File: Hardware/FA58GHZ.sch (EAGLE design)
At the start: 16 parts, among them U1 ATMEGA328P_TQFP, Y1 16MHZ

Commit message: Backup: Working in the Schematic, Footprints and PCB
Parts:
- added C10, C8, C9: 0.1uF, resistor:C-EUC0603
- added IC1: MAX4311EEE, maxim:MAX4311EEE
- added JP3: (no value), SparkFun-Connectors:M06SILK_FEMALE_PTH
- added JP4: (no value), SparkFun-Connectors:M04PTH
- added R10, R11, R12: 1k, resistor:R-US_R0603
- added R5, R6, R7: 10k, resistor:R-US_R0603
- added R8: 470, resistor:R-US_R0603
- added R9: 5k1, resistor:R-US_R0603
- added SG1: BUZZERSMD, SparkFun-Electromechanical:BUZZERSMD
- added U2: RX5808, FreakyAttic-EagleLibrary:RX5808
- added X1: SMA, con-coax:SMA-142-0701-881/886
- JP1: device SparkFun-Connectors:M03PTH -> SparkFun-Connectors:M03SMD
- R3, R4: value 10k -> ?
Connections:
- new net BUT1: U1.PD2(INT0)-D2
- new net BUT2: U1.PD3(INT1)-D3
- new net CH1: R7.1, U1.PB2(SS/OC1B)-D10
- new net CH2: R5.1, U1.PB3(MOSI/OC2)-D11
- new net CH3: R6.1, U1.PB4(MISO)-D12
- new net LED: R2.2, U1.PB5(SCK)-D13
- new net N$10: R12.1, U1.PD5(T1)-D5
- new net N$11: SG1.2, U1.PD6(AIN0)-D6
- new net N$12: R12.2, SG1.1
- new net N$13: R6.2, U2.CH1
- new net N$14: R5.2, U2.CH2
- new net N$15: R7.2, U2.CH3
- new net N$16: U2.ANT, X1.1
- new net N$7: R9.1, U1.PB1(OC1A)-D9
- new net N$8: R10.1, U1.PD0(RXD)-D0
- new net N$9: R11.1, U1.PD1(TXD)-D1
- new net OSD: IC1.IN0, R8.2, R9.2
- new net RSSI1: JP4.2, U1.ADC6-A6, U2.RSSI
- new net RSSI2: JP4.4, U1.ADC7-A7
- new net SEL0: IC1.A0
- new net SEL1: IC1.A1
- new net VIDEO1: IC1.IN1, JP3.2, U2.VIDEO
- new net VIDEO2: IC1.IN2, JP3.4
- new net VIDEO3: IC1.IN3, JP3.6
- new net VIDEO_OUT: IC1.FB, IC1.OUT
- net AN_VPOW: now also C9.2
- net GND: now also C10.1, C8.2, C9.1, IC1.V-, JP3.1, JP3.3, JP3.5, JP4.1, JP4.3, U2.GND@1, U2.GND@2, U2.GND@3, U2.GND@4, X1.2
- net N$6: now also R8.1, U1.PD7(AIN1)-D7; no longer R2.2, U1.PB5(SCK)
- net VCC: now also C10.2, C8.1, IC1.!SHDN, IC1.V+, U2.+5V
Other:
- note added: "1.0"
- note added: "A 5.8GHz video receiver module with OSD menu and multiple video inputs."
- note added: "FA58GHZ.sch"
- moved on the sheet: C1, C4, C5, D1, R1, R2, U1, Y1

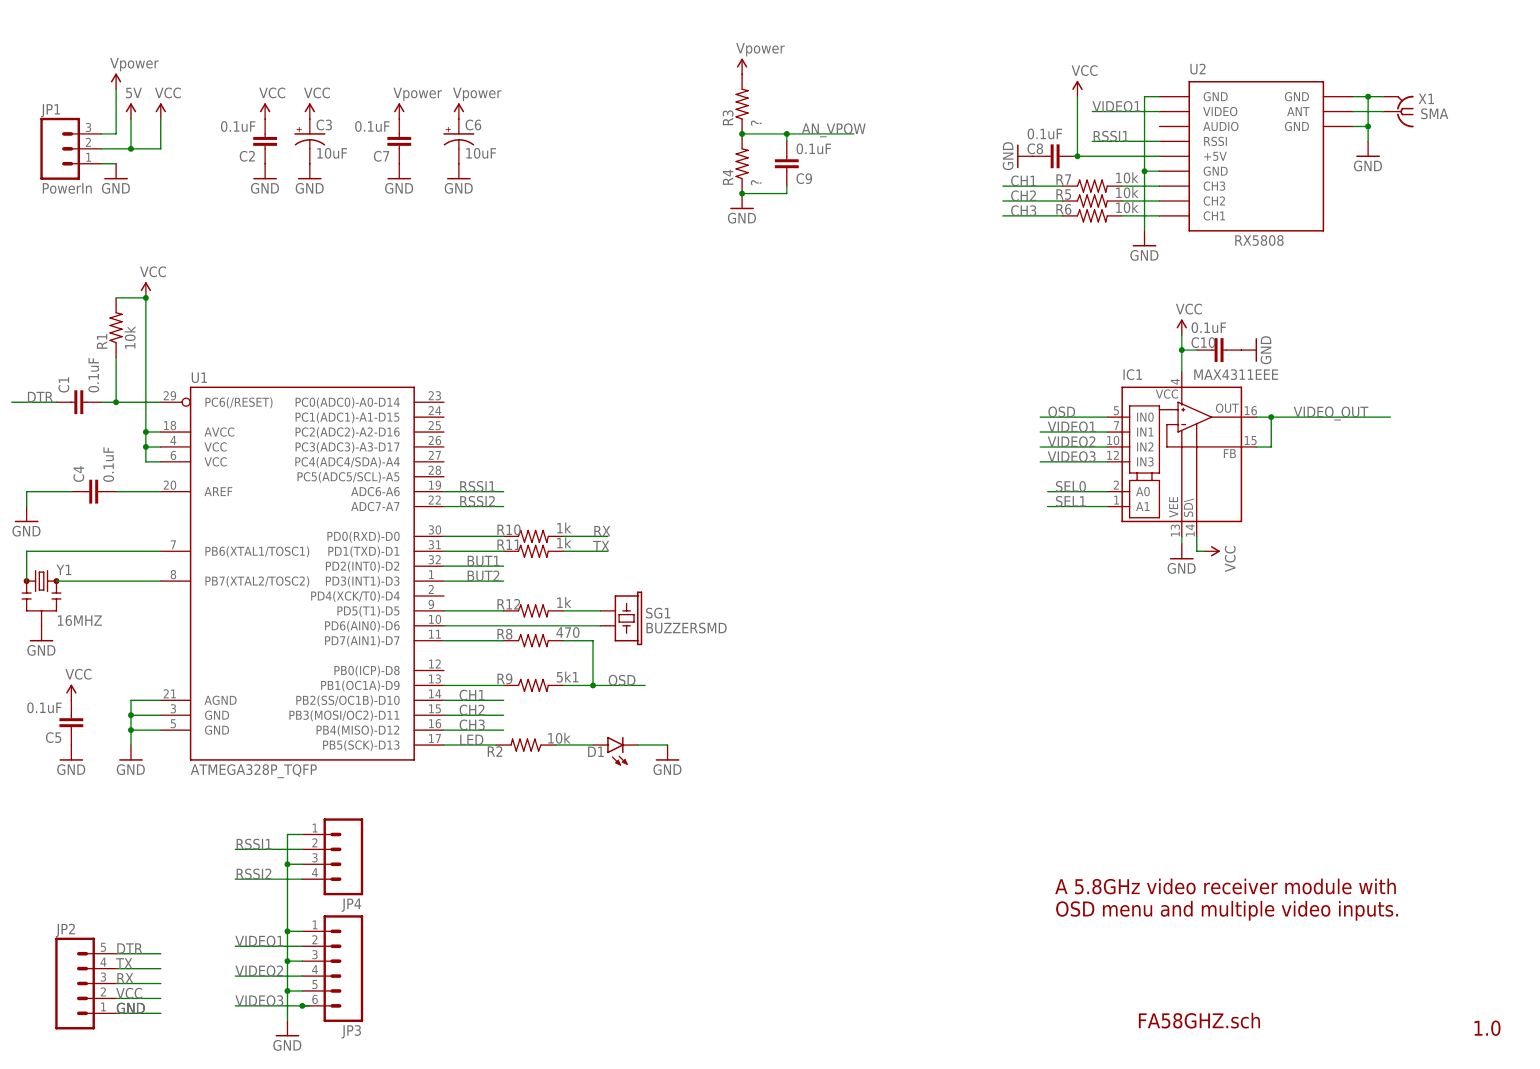
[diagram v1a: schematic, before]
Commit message: Finish with the board Schematic, starting to code functions.
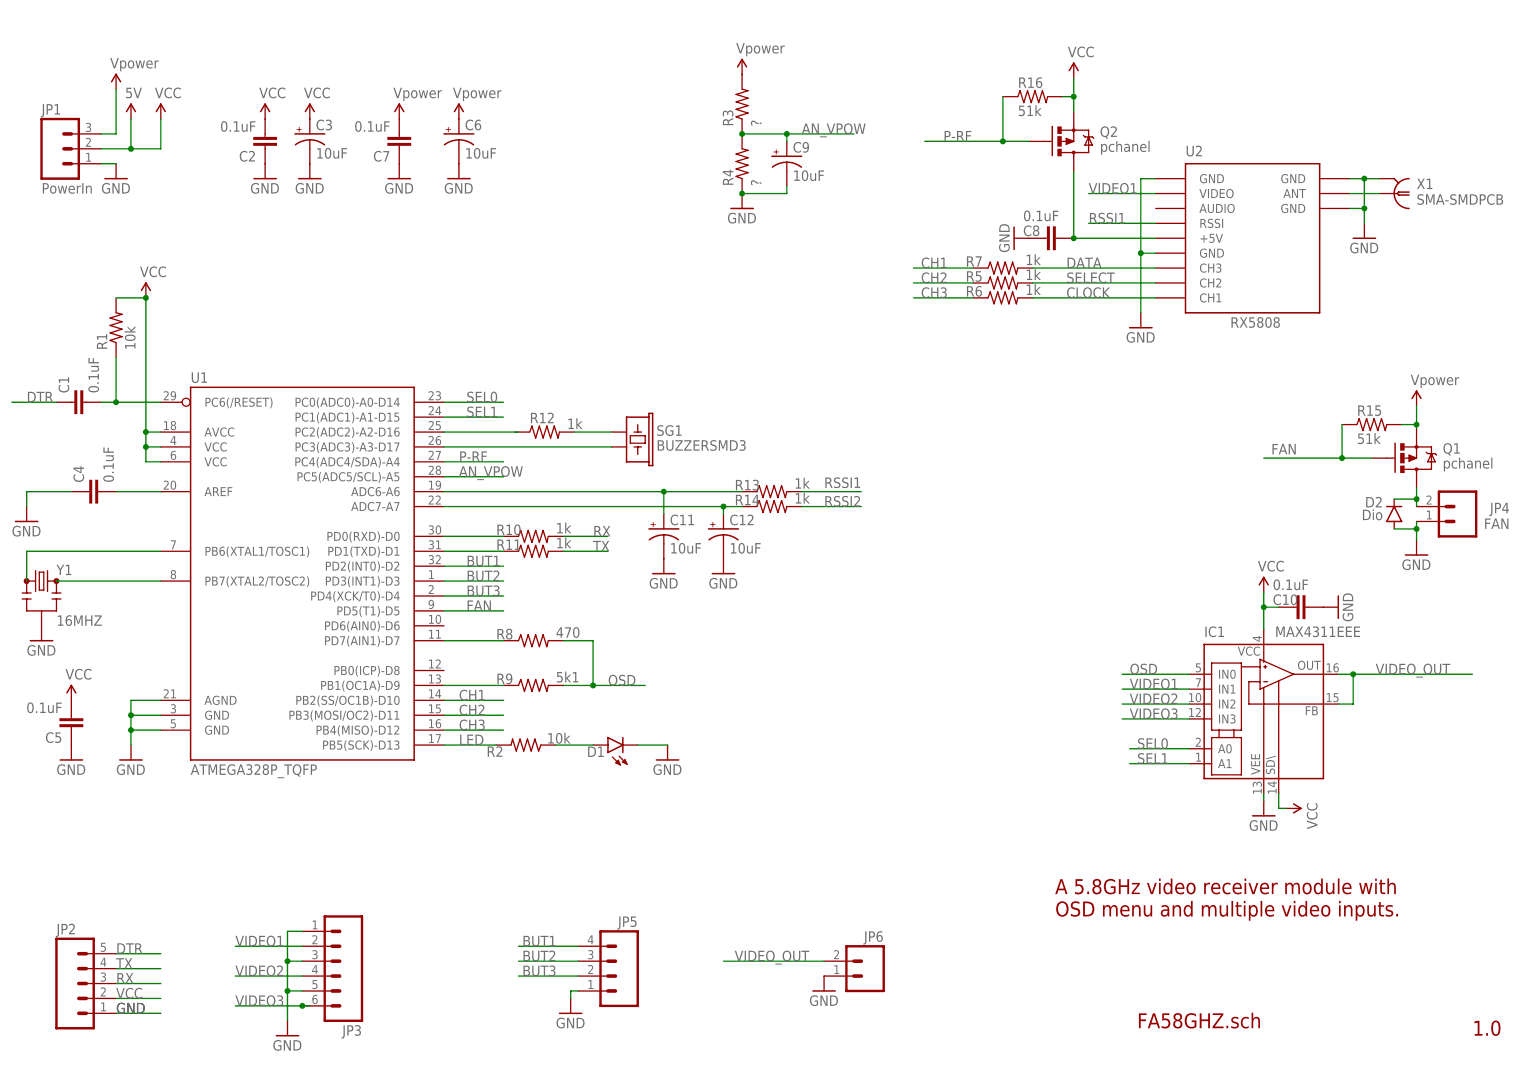
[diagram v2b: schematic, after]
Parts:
- added C11, C12: 10uF, SparkFun-Capacitors:10UF-16V-10%(TANT)
- added D2: Dio, SparkFun-DiscreteSemi:DIODEBAS16
- added JP5: (no value), SparkFun-Connectors:M04PTH
- added JP6: (no value), SparkFun-Connectors:M02PTH
- added Q1, Q2: pchanel, SparkFun-DiscreteSemi:MOSFET-PCHANNEL
- added R13, R14: 1k, resistor:R-US_R0603
- added R15, R16: 51k, resistor:R-US_R0603
- C9: value 0.1uF -> 10uF; device resistor:C-EUC0603 -> SparkFun-Capacitors:10UF-16V-10%(TANT)
- JP4: value (none) -> FAN; device SparkFun-Connectors:M04PTH -> FreakyAttic-EagleLibrary:M02PTH
- R5, R6, R7: value 10k -> 1k
- SG1: value BUZZERSMD -> BUZZERSMD3; device SparkFun-Electromechanical:BUZZERSMD -> FreakyAttic-EagleLibrary:BUZZERSMD3
- X1: value SMA -> SMA-SMDPCB; device con-coax:SMA-142-0701-881/886 -> FreakyAttic-EagleLibrary:SMA-SMDPCB
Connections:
- net N$13 renamed CLOCK
- net N$14 renamed SELECT
- net N$15 renamed DATA
- removed net RSSI2: JP4.4, U1.ADC7-A7
- new net BUT3: JP5.2
- new net FAN: Q1.G, R15.1
- new net N$17: C12.+, R14.1, U1.ADC7-A7
- new net N$18: C11.+, R13.1, U1.ADC6-A6
- new net N$19: D2.C, JP4.2, Q1.D
- new net N$20: C8.1, Q2.D, U2.+5V
- new net P-RF: Q2.G, R16.1
- net AN_VPOW: now also C9.+; no longer C9.2
- net BUT1: now also JP5.4
- net BUT2: now also JP5.3
- net GND: now also C11.-, C12.-, C9.-, D2.A, JP5.1, JP6.1; no longer C9.1, JP4.3
- net N$10: now also U1.PC2(ADC2)-A2-D16; no longer R12.1, U1.PD5(T1)-D5
- net N$11: now also U1.PC3(ADC3)-A3-D17; no longer U1.PD6(AIN0)-D6
- net RSSI1: no longer JP4.2, U1.ADC6-A6
- net VCC: now also Q1.S, Q2.S, R15.2, R16.2; no longer C8.1, U2.+5V
- net VIDEO_OUT: now also JP6.2
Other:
- moved on the sheet: C10, C8, IC1, R12, R5, R6, R7, SG1, U2

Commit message: Backup: Implemented OSD menu for Battery Monitor, needs to test it. - Modifications for the schematic - working on the PCB
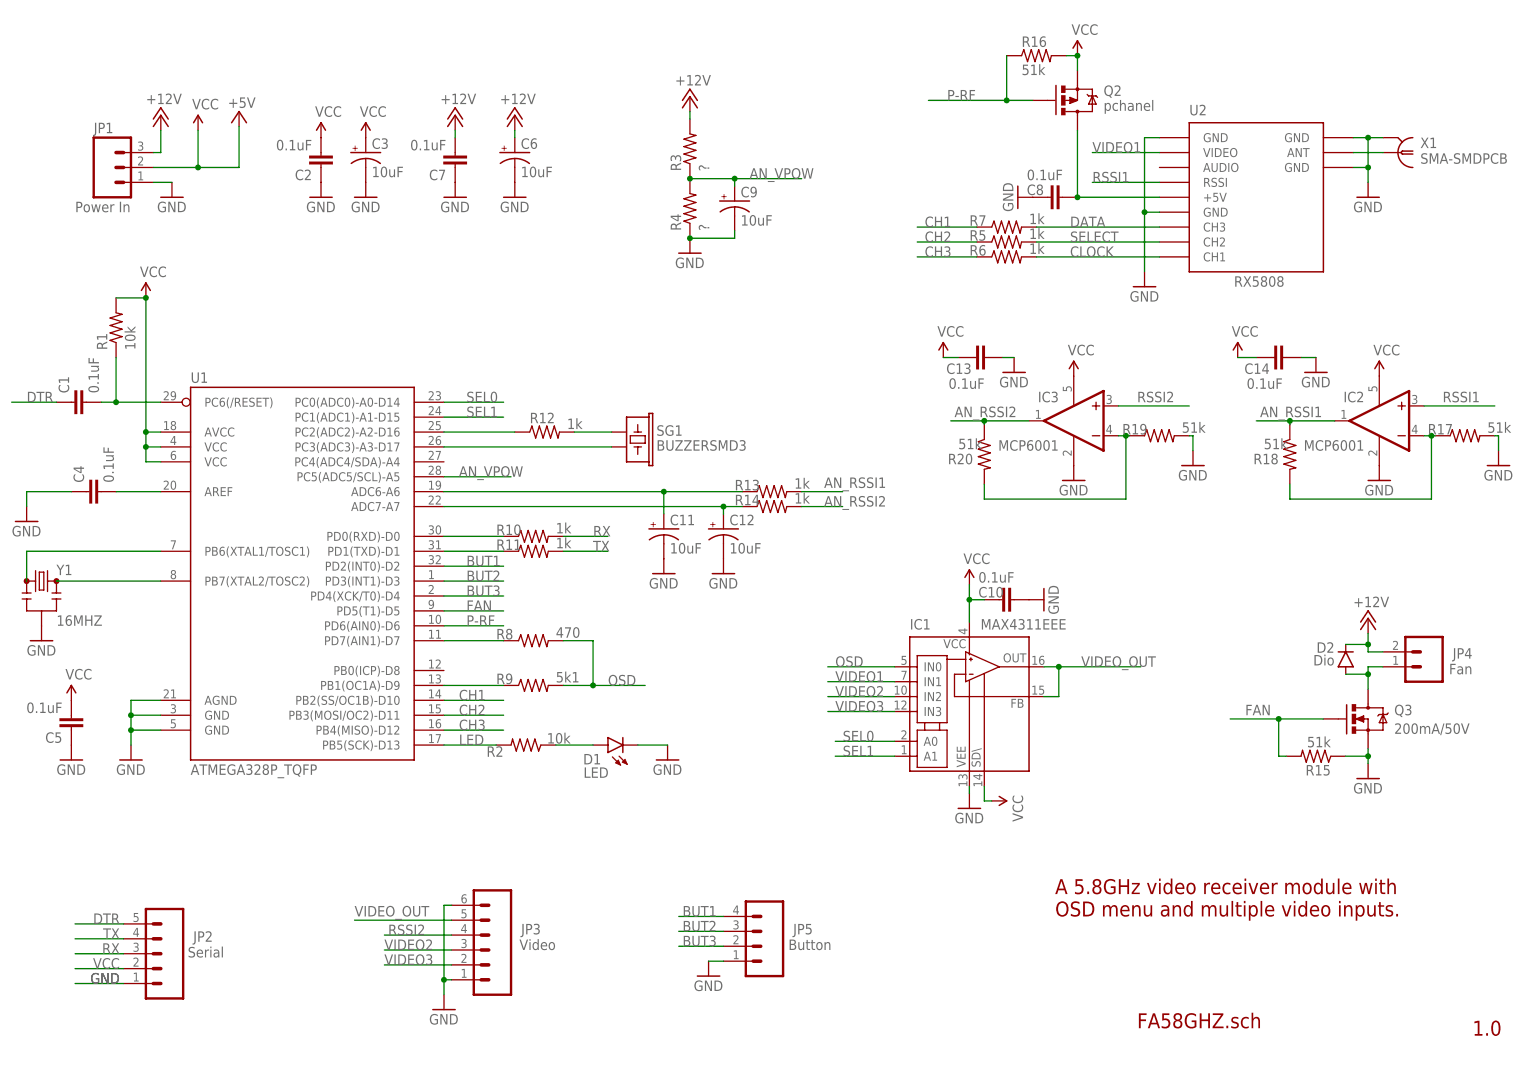
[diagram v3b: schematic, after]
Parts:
- removed JP6: (no value), SparkFun-Connectors:M02PTH
- removed Q1: pchanel, SparkFun-DiscreteSemi:MOSFET-PCHANNEL
- added C13, C14: 0.1uF, resistor:C-EUC0603
- added IC2, IC3: MCP6001, linear:MCP601OT
- added Q3: 200mA/50V, SparkFun-DiscreteSemi:MOSFET-NCHANNELBSS138
- added R17, R18, R19, R20: 51k, resistor:R-US_R0603
- D1: value (none) -> LED
- JP1: value PowerIn -> Power In; device SparkFun-Connectors:M03SMD -> FreakyAttic-EagleLibrary:M03
- JP2: value (none) -> Serial; device SparkFun-Connectors:M05PTH -> FreakyAttic-EagleLibrary:M05
- JP3: value (none) -> Video; device SparkFun-Connectors:M06SILK_FEMALE_PTH -> FreakyAttic-EagleLibrary:M06
- JP4: value FAN -> Fan; device FreakyAttic-EagleLibrary:M02PTH -> FreakyAttic-EagleLibrary:M02
- JP5: value (none) -> Button; device SparkFun-Connectors:M04PTH -> FreakyAttic-EagleLibrary:M04
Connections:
- removed net N$19: D2.C, JP4.2, Q1.D
- new net +12V: C6.+, C7.2, D2.C, JP1.3, JP4.2, R3.2
- new net +5V: JP1.2
- new net AN_RSSI1: IC2.OUT, R13.2, R18.1
- new net AN_RSSI2: IC3.OUT, R14.2, R20.1
- new net N$13: D2.A, JP4.1, Q3.D
- new net N$14: IC2.-IN, R17.1, R18.2
- new net N$15: IC3.-IN, R19.1, R20.2
- new net RSSI2: IC3.+IN, JP3.4
- net AN_VPOW: now also U1.PC5(ADC5/SCL)-A5
- net BUT3: now also U1.PD4(XCK/T0)-D4
- net FAN: now also Q3.G, R15.2, U1.PD5(T1)-D5; no longer Q1.G, R15.1
- net GND: now also C13.2, C14.2, IC2.V-, IC3.V-, JP3.6, Q3.S, R15.1, R17.2, R19.2; no longer D2.A, JP3.3, JP3.5, JP4.1, JP6.1
- net N$10: now also R12.1
- net P-RF: now also U1.PD6(AIN0)-D6
- net RSSI1: now also IC2.+IN
- net RX: now also R10.2
- net SEL0: now also U1.PC0(ADC0)-A0-D14
- net SEL1: now also U1.PC1(ADC1)-A1-D15
- net TX: now also R11.2
- net VCC: now also C13.1, C14.1, IC2.V+, IC3.V+; no longer C6.+, C7.2, JP1.2, JP1.3, Q1.S, R15.2, R3.2
- net VIDEO1: no longer JP3.2
- net VIDEO2: now also JP3.3; no longer JP3.4
- net VIDEO3: now also JP3.2; no longer JP3.6
- net VIDEO_OUT: now also JP3.5; no longer JP6.2
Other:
- moved on the sheet: C10, C2, C3, C6, C7, C8, C9, D2, IC1, JP1, JP2, JP3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

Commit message: Backup: PCB routing finished, need to run DRC
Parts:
- C11, C12, C9: device SparkFun-Capacitors:10UF-16V-10%(TANT) -> SparkFun-Passives:CAP0603-CAP
- Y1: device SparkFun-FreqCtrl:RESONATOR16MHZ -> FreakyAttic-EagleLibrary:OSCILLATOR16MHZ
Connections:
- removed net +5V: JP1.2
- net AN_VPOW: now also C9.1; no longer C9.+
- net BUT1: now also JP5.2; no longer JP5.4
- net BUT3: now also JP5.4; no longer JP5.2
- net GND: now also C11.2, C12.2, C9.2; no longer C11.-, C12.-, C9.-
- net N$17: now also C12.1; no longer C12.+
- net N$18: now also C11.1; no longer C11.+
- net RSSI2: now also JP3.5; no longer JP3.4
- net VCC: now also JP1.2
- net VIDEO2: now also JP3.2; no longer JP3.3
- net VIDEO3: now also JP3.3; no longer JP3.2
- net VIDEO_OUT: now also JP3.4; no longer JP3.5

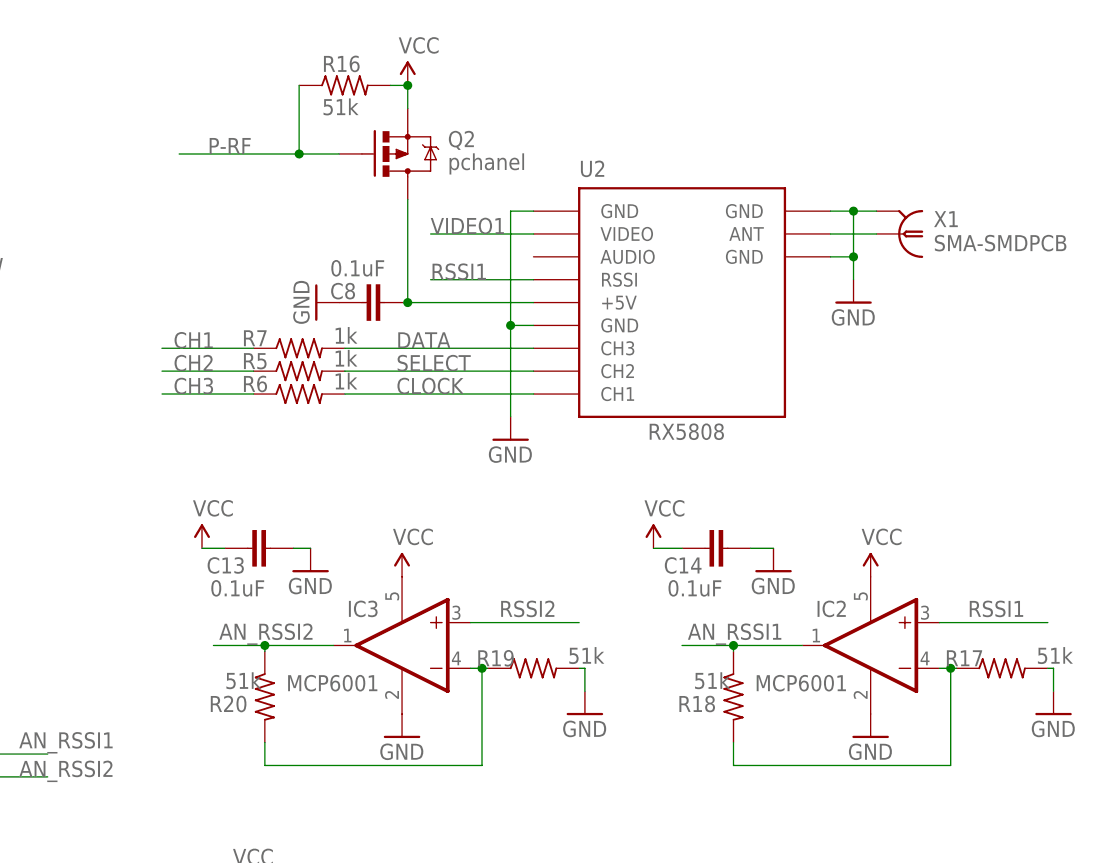
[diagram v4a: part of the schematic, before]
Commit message: BOARD VER: 1.1 - Fix footprints and pinout problems with RF
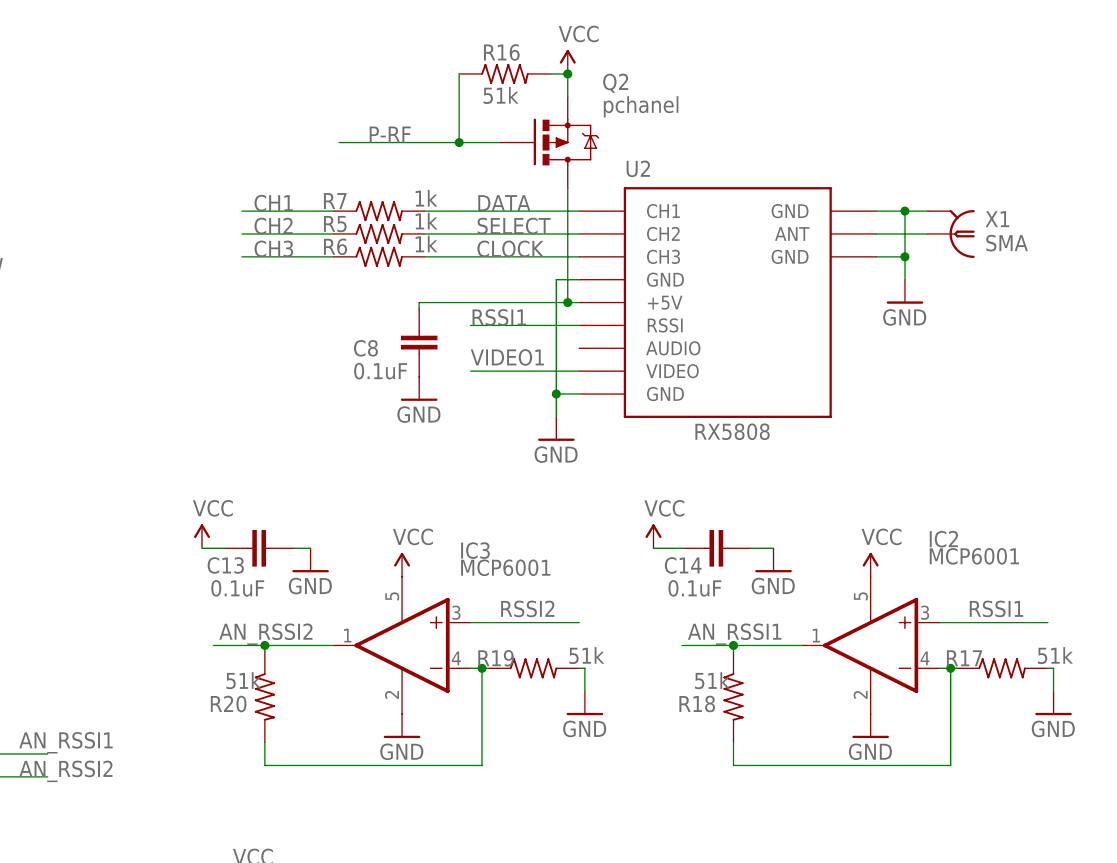
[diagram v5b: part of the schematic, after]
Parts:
- IC1: device maxim:MAX4311EEE -> FreakyAttic-EagleLibrary:MAX4311EEE
- IC2, IC3: device linear:MCP601OT -> FreakyAttic-EagleLibrary:MCP6001
- X1: value SMA-SMDPCB -> SMA
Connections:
- net CLOCK: now also U2.CH3; no longer U2.CH1
- net DATA: now also U2.CH1; no longer U2.CH3
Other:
- moved on the sheet: C8, Q2, R16, R5, R6, R7, U2, X1
